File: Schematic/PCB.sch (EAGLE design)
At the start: 68 parts, among them J1 POWER_JACK, U1 V_REG_317SINK

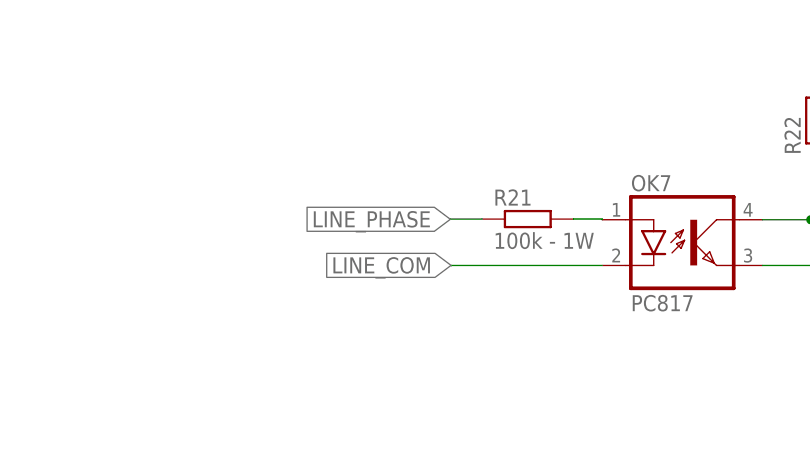
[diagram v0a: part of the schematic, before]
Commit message: added protection diode on zero cross detector
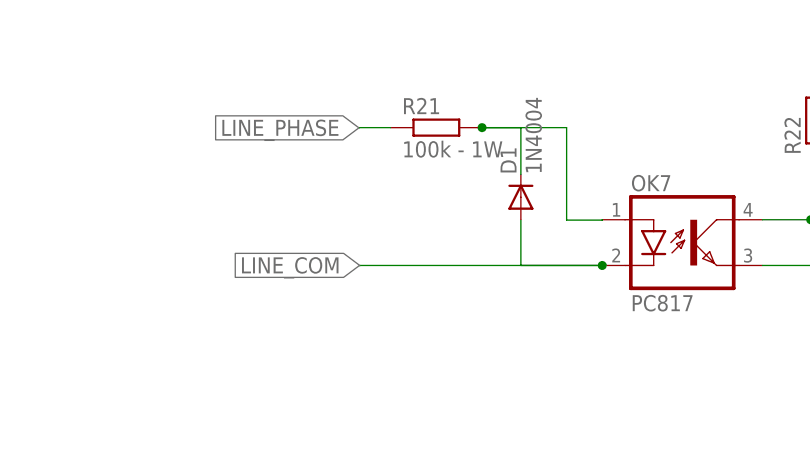
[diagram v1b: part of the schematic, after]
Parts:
- added D1: 1N4004, adafruit:1N4004
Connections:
- net LINE_COM: now also D1.A
- net N$14: now also D1.C
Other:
- moved on the sheet: R21
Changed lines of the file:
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@@
 <setting verticaltext="up"/>
 </settings>
-<grid distance="0.1" unitdist="inch" unit="inch" style="lines" multiple="1" display="no" altdistance="0.01" altunitdist="inch" altunit="inch"/>
+<grid distance="0.1" unitdist="mm" unit="mm" style="lines" multiple="1" display="no" altdistance="0.01" altunitdist="mm" altunit="mm"/>
 <layers>
 <layer number="1" name="Top" color="4" fill="1" visible="no" active="no"/>
@@
 <part name="GND10" library="supply1" library_urn="urn:adsk.eagle:library:371" deviceset="GND" device=""/>
 <part name="GND11" library="supply1" library_urn="urn:adsk.eagle:library:371" deviceset="GND" device=""/>
+<part name="D1" library="adafruit" library_urn="urn:adsk.eagle:library:420" deviceset="1N4004" device="" package3d_urn="urn:adsk.eagle:package:6240344/1"/>
 </parts>
 <sheets>
@@
 <attribute name="VALUE" x="300.55861875" y="62.555115625" size="1.778" layer="96" rot="R90"/>
 </instance>
-<instance part="R21" gate="G$1" x="305.565115625" y="190.61338125" smashed="yes">
-<attribute name="NAME" x="301.755115625" y="192.11198125" size="1.778" layer="95"/>
-<attribute name="VALUE" x="301.755115625" y="187.31138125" size="1.778" layer="96"/>
+<instance part="R21" gate="G$1" x="295.405115625" y="200.77338125" smashed="yes">
+<attribute name="NAME" x="291.595115625" y="202.27198125" size="1.778" layer="95"/>
+<attribute name="VALUE" x="291.595115625" y="197.47138125" size="1.778" layer="96"/>
 </instance>
 <instance part="R22" gate="G$1" x="337.38661875" y="201.565115625" smashed="yes" rot="R90">
@@
 <instance part="GND11" gate="1" x="265.01" y="89.25" smashed="yes">
 <attribute name="VALUE" x="262.47" y="86.71" size="1.778" layer="96"/>
+</instance>
+<instance part="D1" gate="1" x="304.8" y="193.04" smashed="yes" rot="R90">
+<attribute name="NAME" x="304.3174" y="195.58" size="1.778" layer="95" rot="R90"/>
+<attribute name="VALUE" x="307.1114" y="195.58" size="1.778" layer="96" rot="R90"/>
 </instance>
 </instances>
@@
 <segment>
 <pinref part="R21" gate="G$1" pin="1"/>
-<wire x1="300.485115625" y1="190.61338125" x2="296.98" y2="190.61338125" width="0.1524" layer="91"/>
-<wire x1="296.98" y1="190.61338125" x2="296.98" y2="190.6" width="0.1524" layer="91"/>
-<label x="296.96" y="190.59" size="1.778" layer="95" rot="R180" xref="yes"/>
+<wire x1="290.325115625" y1="200.77338125" x2="286.82" y2="200.77338125" width="0.1524" layer="91"/>
+<wire x1="286.82" y1="200.77338125" x2="286.82" y2="200.76" width="0.1524" layer="91"/>
+<label x="286.8" y="200.75" size="1.778" layer="95" rot="R180" xref="yes"/>
 </segment>
 <segment>
@@
 </segment>
 </net>
-<net name="N$14" class="0">
-<segment>
-<pinref part="R21" gate="G$1" pin="2"/>
-<wire x1="310.645115625" y1="190.61338125" x2="310.645115625" y2="190.62" width="0.1524" layer="91"/>
-<wire x1="310.645115625" y1="190.62" x2="313.84" y2="190.62" width="0.1524" layer="91"/>
-<pinref part="OK7" gate="A" pin="A"/>
-<wire x1="313.84" y1="190.62" x2="313.84" y2="190.54" width="0.1524" layer="91"/>
-</segment>
-</net>
 <net name="LINE_COM" class="0">
 <segment>
 <pinref part="OK7" gate="A" pin="C"/>
-<wire x1="313.84" y1="185.46" x2="297.06" y2="185.46" width="0.1524" layer="91"/>
-<wire x1="297.06" y1="185.46" x2="297.06" y2="185.42" width="0.1524" layer="91"/>
-<label x="297.04" y="185.47" size="1.778" layer="95" rot="R180" xref="yes"/>
+<wire x1="313.84" y1="185.46" x2="286.9" y2="185.46" width="0.1524" layer="91"/>
+<wire x1="286.9" y1="185.46" x2="286.9" y2="185.42" width="0.1524" layer="91"/>
+<label x="286.88" y="185.47" size="1.778" layer="95" rot="R180" xref="yes"/>
+<pinref part="D1" gate="1" pin="A"/>
+<wire x1="313.84" y1="185.46" x2="304.8" y2="185.46" width="0.1524" layer="91"/>
+<wire x1="304.8" y1="185.46" x2="304.8" y2="190.5" width="0.1524" layer="91"/>
+<junction x="313.84" y="185.46"/>
 </segment>
 <segment>
@@
 </segment>
 </net>
+<net name="N$14" class="0">
+<segment>
+<pinref part="R21" gate="G$1" pin="2"/>
+<wire x1="300.485115625" y1="200.77338125" x2="309.88" y2="200.77338125" width="0.1524" layer="91"/>
+<wire x1="309.88" y1="200.77338125" x2="309.88" y2="190.5" width="0.1524" layer="91"/>
+<pinref part="OK7" gate="A" pin="A"/>
+<wire x1="309.88" y1="190.5" x2="313.84" y2="190.5" width="0.1524" layer="91"/>
+<wire x1="313.84" y1="190.5" x2="313.84" y2="190.54" width="0.1524" layer="91"/>
+<pinref part="D1" gate="1" pin="C"/>
+<wire x1="300.485115625" y1="200.77338125" x2="304.8" y2="200.77338125" width="0.1524" layer="91"/>
+<wire x1="304.8" y1="200.77338125" x2="304.8" y2="195.58" width="0.1524" layer="91"/>
+<junction x="300.485115625" y="200.77338125"/>
+</segment>
+</net>
